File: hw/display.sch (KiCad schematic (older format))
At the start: 22 parts, among them J1 AMPSEAL_8_POS_776275-1, J4 HEADER_MOLEX_52207-0433, J5 HEADER_MOLEX_54104-4031, U1 MCP2551_SOIC8, U2 ALLIANCE_AS4C4M16SA_TSOP_II, U3 WINDBOND_W25Q32FV_SOIC8_W, U6 MOSFET-N_2N7002W, X2 XTAL_ABS25-32.768KHZ-T, X3 BUZZER_PKM13EPYH4002-B0

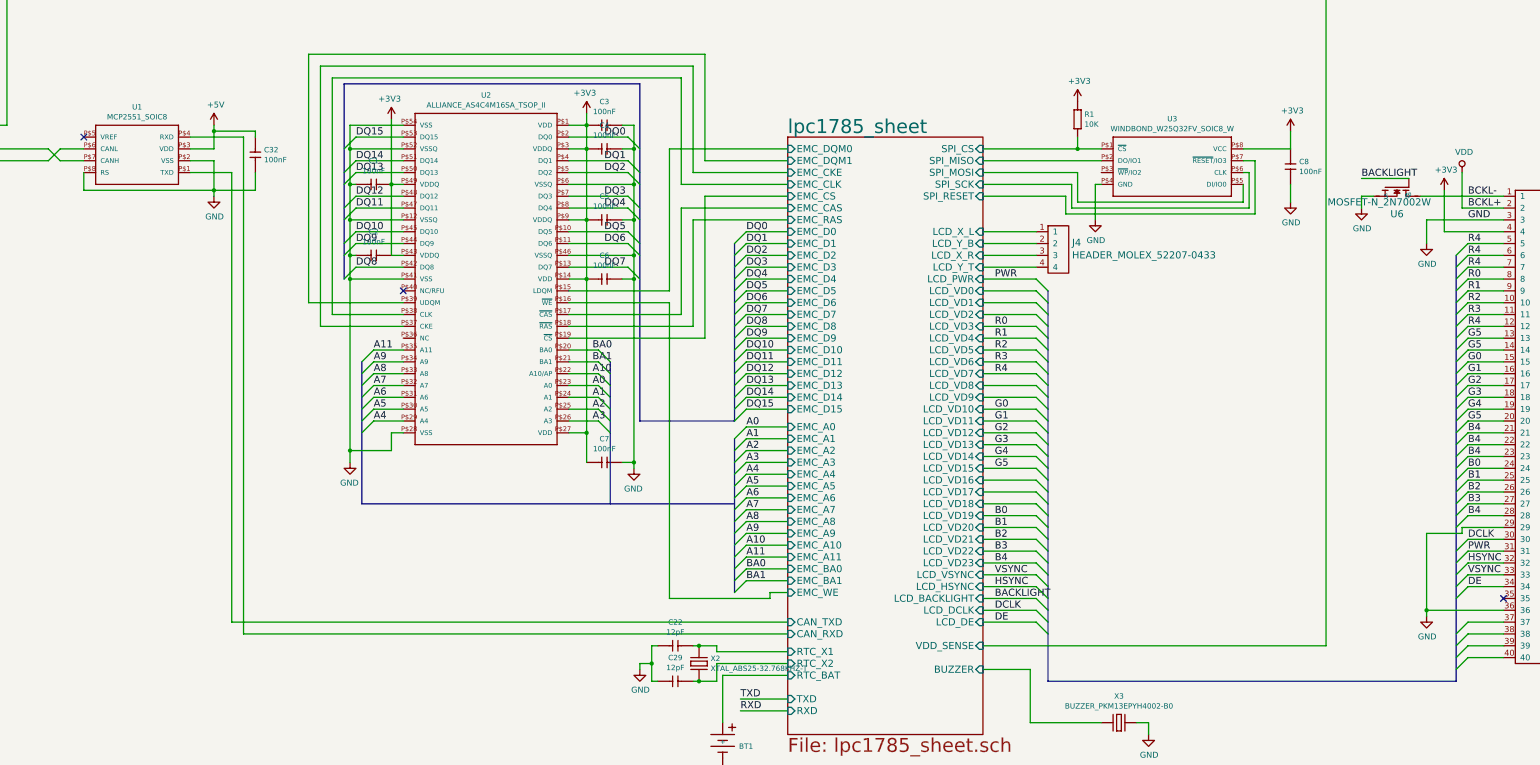
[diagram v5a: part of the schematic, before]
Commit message: Implementing notifications. not tested!
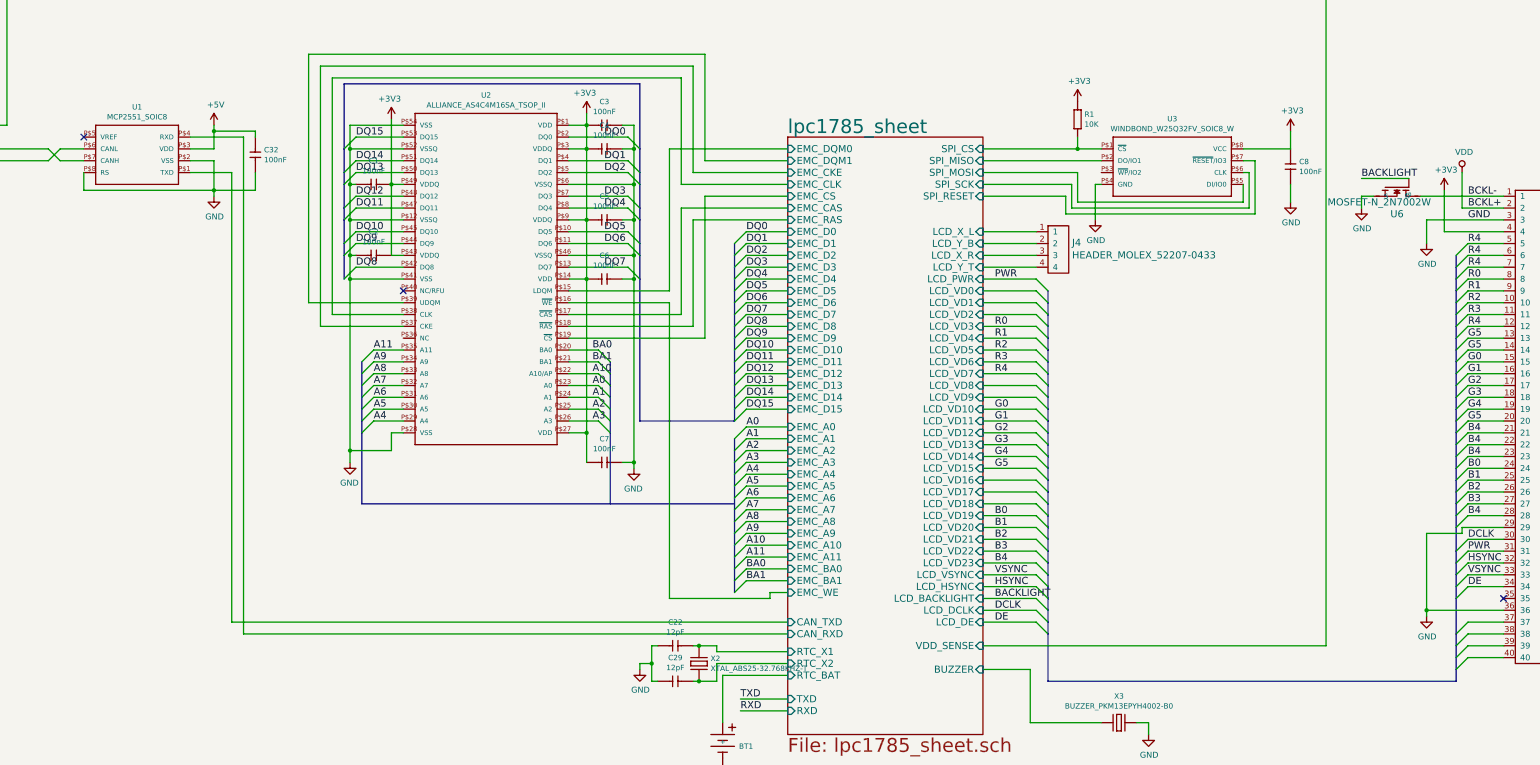
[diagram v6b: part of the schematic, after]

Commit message: multiple bug fixes, uv terminal SDO interface
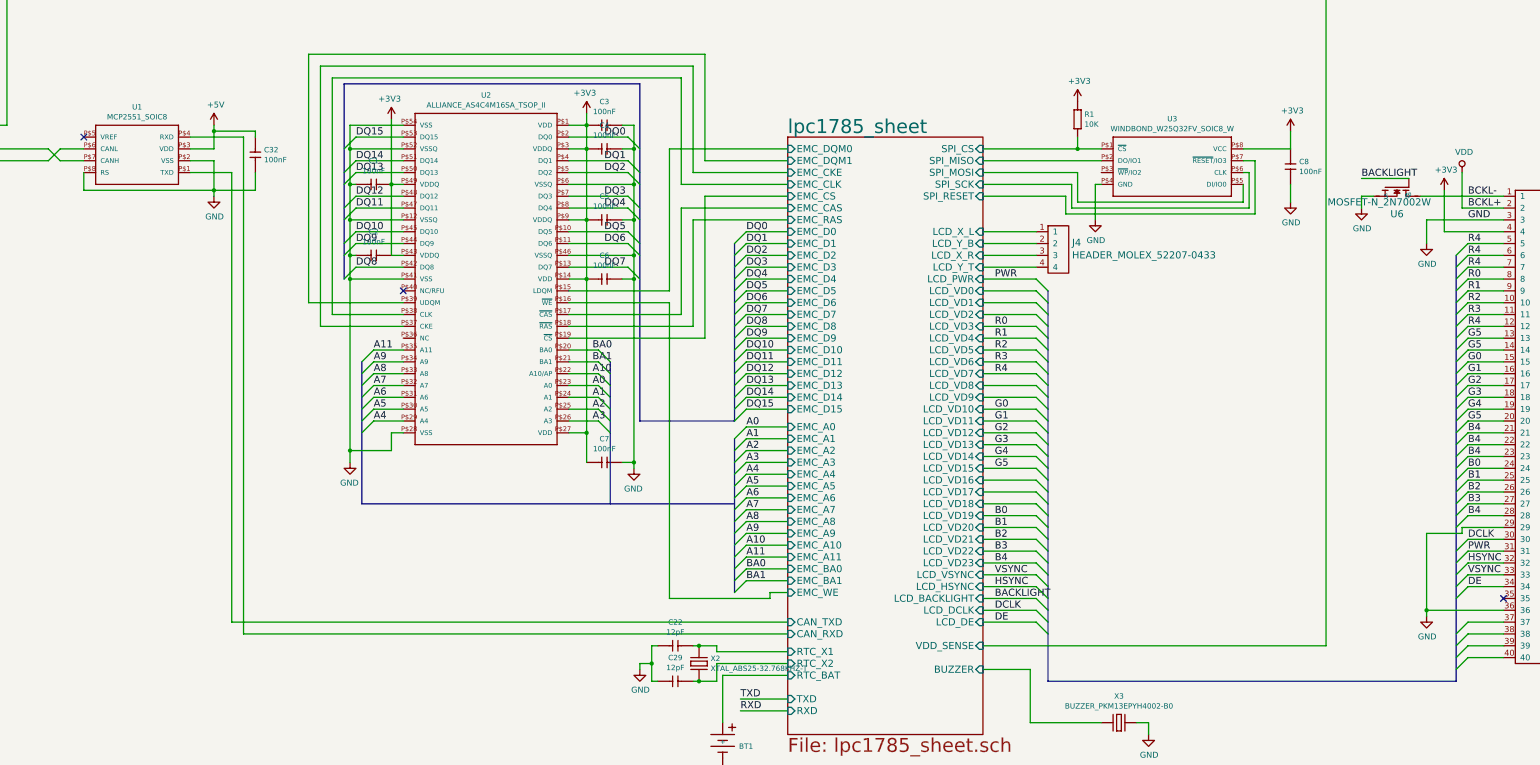
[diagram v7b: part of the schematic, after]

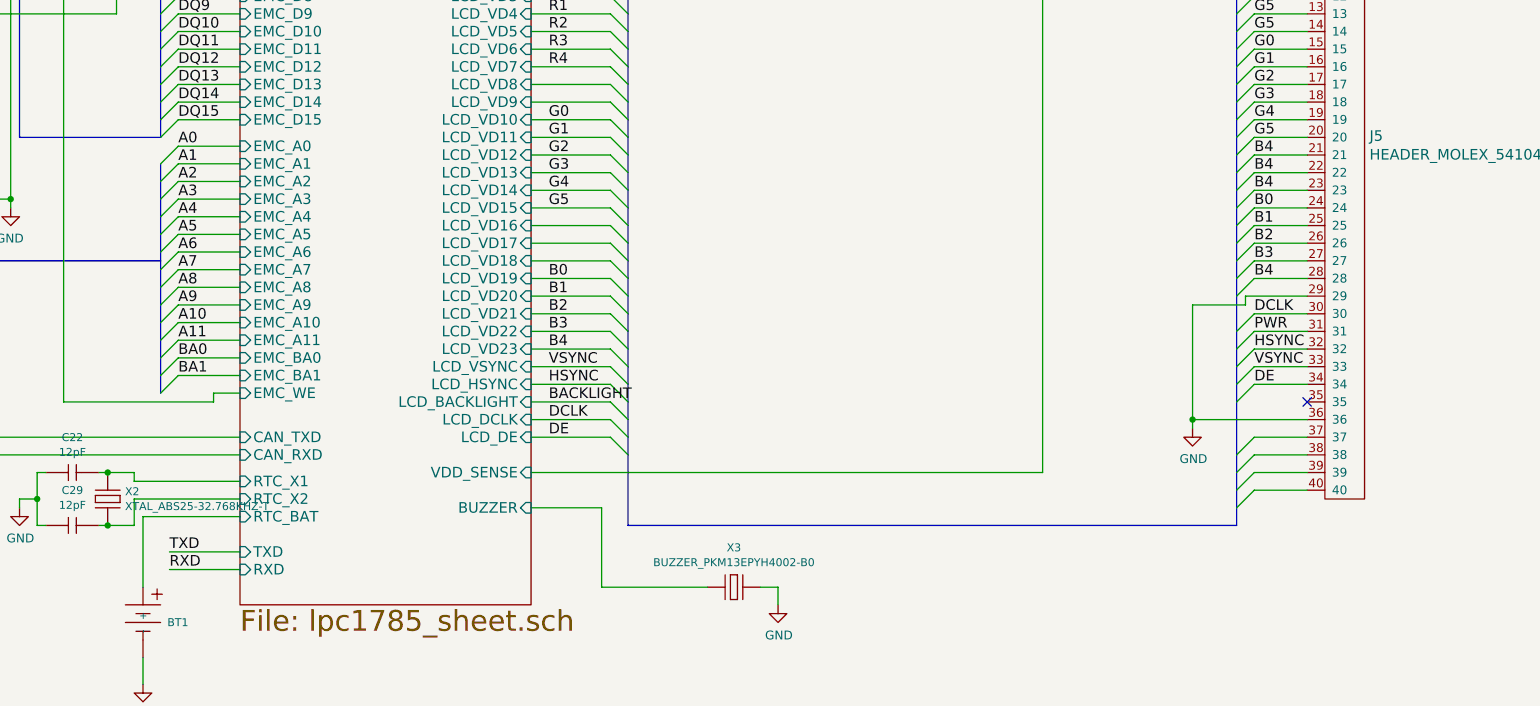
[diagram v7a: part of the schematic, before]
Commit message: starting to design hw 5.0, with variable current source for LCD backlight
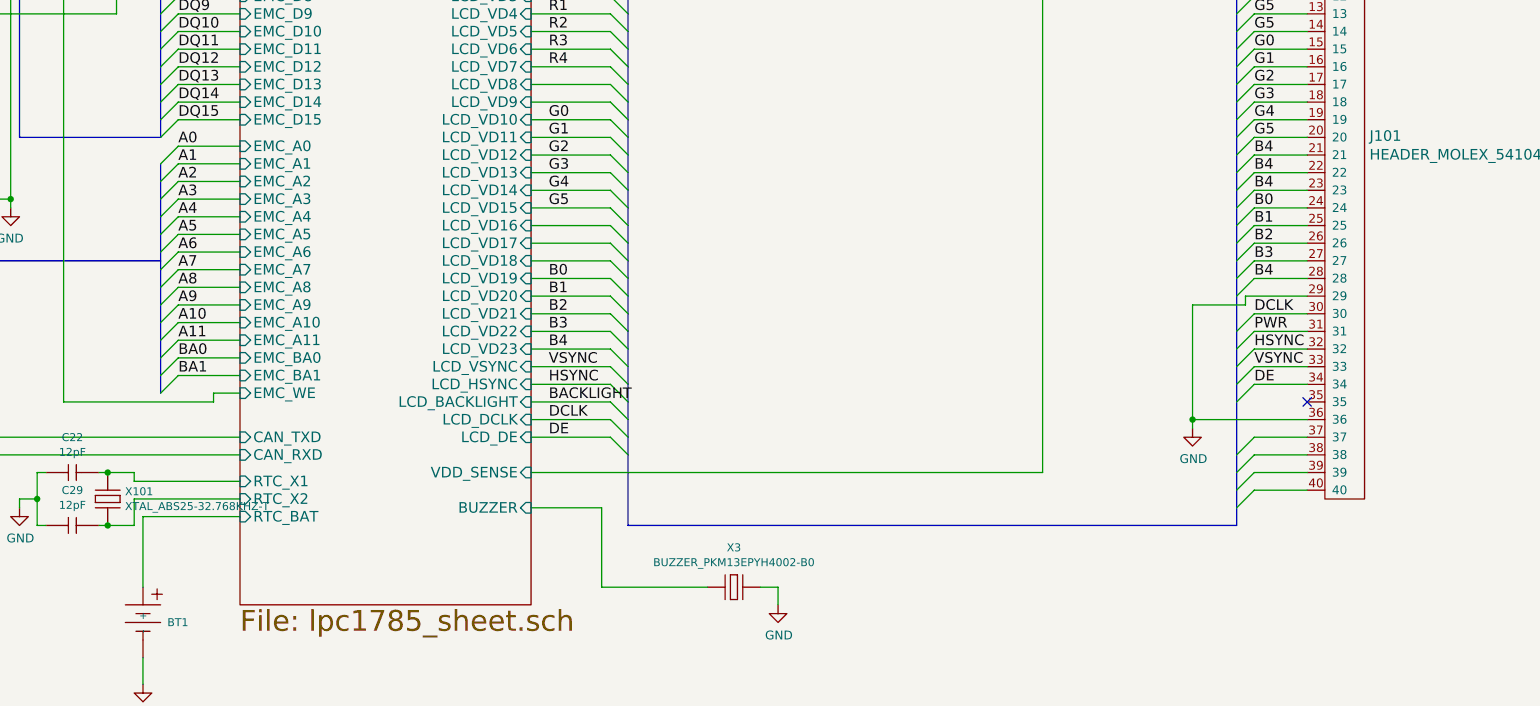
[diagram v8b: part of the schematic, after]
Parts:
- removed J5: HEADER_MOLEX_54104-4031, usevolt:HEADER_MOLEX_54104-4031, symbol HEADER_MOLEX_54104-4031
- removed X2: XTAL_ABS25-32.768KHZ-T, usevolt:XTAL_32.768KHZ-T, symbol XTAL_ABS25-32.768KHZ-T
- added J101: HEADER_MOLEX_54104-4031, usevolt:HEADER_MOLEX_54104-4031, symbol HEADER_MOLEX_54104-4031
- added X101: XTAL_ABS25-32.768KHZ-T, usevolt:XTAL_32.768KHZ-T, symbol XTAL_ABS25-32.768KHZ-T
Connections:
- net +3V3: now also J101.4
- net B0: now also J101.24
- net B1: now also J101.25
- net B2: now also J101.26
- net B3: now also J101.27
- net B4: now also J101.21, J101.22, J101.23, J101.28
- net BCKL-: now also J101.1
- net DCLK: now also J101.30
- net DE: now also J101.34
- net G0: now also J101.15
- net G1: now also J101.16
- net G2: now also J101.17
- net G3: now also J101.18
- net G4: now also J101.19
- net G5: now also J101.13, J101.14, J101.20
- net GND: now also J101.29, J101.3, J101.36
- net HSYNC: now also J101.32
- net PWR: now also J101.31
- net R0: now also J101.8
- net R1: now also J101.9
- net R2: now also J101.10
- net R3: now also J101.11
- net R4: now also J101.12, J101.5, J101.6, J101.7
- net VDD: now also J101.2
- net VSYNC: now also J101.33
- net lpc1785_sheet/RTC_X1: now also X101.1 (P$1)
- net lpc1785_sheet/RTC_X2: now also X101.4 (P$2)
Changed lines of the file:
@@
 $EndComp
 $Comp
-L +5V #PWR01
+L +5V #PWR101
 U 1 1 57BD825A
 P 3200 3000
-F 0 "#PWR01" H 3200 2850 50  0001 C CNN
+F 0 "#PWR101" H 3200 2850 50  0001 C CNN
 F 1 "+5V" H 3215 3173 50  0000 C CNN
 F 2 "" H 3200 3000 50  0000 C CNN
@@
 $EndComp
 $Comp
-L GND #PWR02
+L GND #PWR102
 U 1 1 57BD84BA
 P 3200 3600
-F 0 "#PWR02" H 3200 3350 50  0001 C CNN
+F 0 "#PWR102" H 3200 3350 50  0001 C CNN
 F 1 "GND" H 3205 3427 50  0000 C CNN
 F 2 "" H 3200 3600 50  0000 C CNN
@@
 $EndComp
 $Comp
-L +3V3 #PWR03
+L +3V3 #PWR105
 U 1 1 57C0A187
 P 6350 2900
-F 0 "#PWR03" H 6350 2750 50  0001 C CNN
+F 0 "#PWR105" H 6350 2750 50  0001 C CNN
 F 1 "+3V3" H 6365 3073 50  0000 C CNN
 F 2 "" H 6350 2900 50  0000 C CNN
@@
 $EndComp
 $Comp
-L +3V3 #PWR04
+L +3V3 #PWR104
 U 1 1 57C0A3E9
 P 4700 2950
-F 0 "#PWR04" H 4700 2800 50  0001 C CNN
+F 0 "#PWR104" H 4700 2800 50  0001 C CNN
 F 1 "+3V3" H 4715 3123 50  0000 C CNN
 F 2 "" H 4700 2950 50  0000 C CNN
@@
 $EndComp
 $Comp
-L GND #PWR05
+L GND #PWR106
 U 1 1 57C0A773
 P 6750 5900
-F 0 "#PWR05" H 6750 5650 50  0001 C CNN
+F 0 "#PWR106" H 6750 5650 50  0001 C CNN
 F 1 "GND" H 6755 5727 50  0000 C CNN
 F 2 "" H 6750 5900 50  0000 C CNN
@@
 $EndComp
 $Comp
-L GND #PWR06
+L GND #PWR103
 U 1 1 57C0BFBA
 P 4350 5850
-F 0 "#PWR06" H 4350 5600 50  0001 C CNN
+F 0 "#PWR103" H 4350 5600 50  0001 C CNN
 F 1 "GND" H 4355 5677 50  0000 C CNN
 F 2 "" H 4350 5850 50  0000 C CNN
@@
 $EndComp
 $Comp
-L GND #PWR07
+L GND #PWR110
 U 1 1 57C58382
 P 10650 3800
-F 0 "#PWR07" H 10650 3550 50  0001 C CNN
+F 0 "#PWR110" H 10650 3550 50  0001 C CNN
 F 1 "GND" H 10655 3627 50  0000 C CNN
 F 2 "" H 10650 3800 50  0000 C CNN
@@
 $EndComp
 $Comp
-L +3V3 #PWR08
+L +3V3 #PWR112
 U 1 1 57C588D1
 P 12300 3050
-F 0 "#PWR08" H 12300 2900 50  0001 C CNN
+F 0 "#PWR112" H 12300 2900 50  0001 C CNN
 F 1 "+3V3" H 12315 3223 50  0000 C CNN
 F 2 "" H 12300 3050 50  0000 C CNN
@@
 $EndComp
 $Comp
-L GND #PWR09
+L GND #PWR113
 U 1 1 57C596F8
 P 12300 3650
-F 0 "#PWR09" H 12300 3400 50  0001 C CNN
+F 0 "#PWR113" H 12300 3400 50  0001 C CNN
 F 1 "GND" H 12305 3477 50  0000 C CNN
 F 2 "" H 12300 3650 50  0000 C CNN
@@
 $EndComp
 $Comp
-L +3V3 #PWR010
+L +3V3 #PWR109
 U 1 1 57C5A7BF
 P 10500 2800
-F 0 "#PWR010" H 10500 2650 50  0001 C CNN
+F 0 "#PWR109" H 10500 2650 50  0001 C CNN
 F 1 "+3V3" H 10515 2973 50  0000 C CNN
 F 2 "" H 10500 2800 50  0000 C CNN
@@
 GND
 $Comp
-L +3V3 #PWR011
+L +3V3 #PWR117
 U 1 1 57BF31A5
 P 13600 3550
-F 0 "#PWR011" H 13600 3400 50  0001 C CNN
+F 0 "#PWR117" H 13600 3400 50  0001 C CNN
 F 1 "+3V3" H 13615 3723 50  0000 C CNN
 F 2 "" H 13600 3550 50  0000 C CNN
@@
 $EndComp
 $Comp
-L GND #PWR012
+L GND #PWR115
 U 1 1 57BF38B7
 P 13450 4000
-F 0 "#PWR012" H 13450 3750 50  0001 C CNN
+F 0 "#PWR115" H 13450 3750 50  0001 C CNN
 F 1 "GND" H 13455 3827 50  0000 C CNN
 F 2 "" H 13450 4000 50  0000 C CNN
@@
 B4
 $Comp
-L GND #PWR013
+L GND #PWR116
 U 1 1 57BFF748
 P 13450 7150
-F 0 "#PWR013" H 13450 6900 50  0001 C CNN
+F 0 "#PWR116" H 13450 6900 50  0001 C CNN
 F 1 "GND" H 13455 6977 50  0000 C CNN
 F 2 "" H 13450 7150 50  0000 C CNN
@@
 NoConn ~ 14100 7000
 $Comp
-L VDD #PWR014
+L VDD #PWR118
 U 1 1 57C283B6
 P 13750 3400
-F 0 "#PWR014" H 13750 3250 50  0001 C CNN
+F 0 "#PWR118" H 13750 3250 50  0001 C CNN
 F 1 "VDD" H 13767 3573 50  0000 C CNN
 F 2 "" H 13750 3400 50  0000 C CNN
@@
 F79 "RTC_X1" I L 8050 7450 60
 F80 "VDD_SENSE" I R 9700 7400 60
-F81 "TXD" I L 8050 7850 60
-F82 "RXD" I L 8050 7950 60
 F83 "SPI_MOSI" I R 9700 3400 60
 F84 "SPI_MISO" I R 9700 3300 60
@@
 $EndComp
 $Comp
-L HEADER_MOLEX_54104-4031 J5
-U 1 1 57C476E2
-P 14250 5050
-F 0 "J5" H 14453 4608 60  0000 L CNN
-F 1 "HEADER_MOLEX_54104-4031" H 14453 4502 60  0000 L CNN
-F 2 "usevolt:HEADER_MOLEX_54104-4031" H 14350 6700 60  0001 C CNN
-F 3 "http://www.farnell.com/datasheets/1875244.pdf?_ga=1.223199835.1948984246.1460023966" H 14225 7025 60  0001 C CNN
-F 4 "1757126" H 14125 6975 60  0001 C CNN "1st Source Part Number"
-F 5 "54104-4031" H 14100 6850 60  0001 C CNN "Manufacturer Part Number"
-F 6 "Farnell" H 14125 6925 60  0001 C CNN "1st Source"
-F 7 "MOLEX" H 14125 6775 60  0001 C CNN "Manufacturer"
-	1    14250 5050
-	1    0    0    -1
-$EndComp
-$Comp
 L BATTERY_HOLDER_CH7410-2032LFSMD BT1
 U 1 1 57C449B5
@@
 $EndComp
 $Comp
-L GND #PWR015
+L GND #PWR108
 U 1 1 57C44DCF
 P 7500 8600
-F 0 "#PWR015" H 7500 8350 50  0001 C CNN
+F 0 "#PWR108" H 7500 8350 50  0001 C CNN
 F 1 "GND" H 7505 8427 50  0000 C CNN
 F 2 "" H 7500 8600 50  0000 C CNN
@@
 $EndComp
 $Comp
-L GND #PWR016
+L GND #PWR107
 U 1 1 57C4DF04
 P 6800 7600
-F 0 "#PWR016" H 6800 7350 50  0001 C CNN
+F 0 "#PWR107" H 6800 7350 50  0001 C CNN
 F 1 "GND" H 6805 7427 50  0000 C CNN
 F 2 "" H 6800 7600 50  0000 C CNN
@@
 	1    6800 7600
 	1    0    0    -1
-$EndComp
-$Comp
-L XTAL_ABS25-32.768KHZ-T X2
-U 1 1 57C465F9
-P 7300 7600
-F 0 "X2" V 7208 7698 45  0000 L CNN
-F 1 "XTAL_ABS25-32.768KHZ-T" V 7292 7698 45  0000 L CNN
-F 2 "usevolt:XTAL_32.768KHZ-T" H 7330 7750 20  0001 C CNN
-F 3 "http://www.abracon.com/Resonators/abs25.pdf" H 7320 7620 60  0001 C CNN
-F 4 "1611824" H 7920 8220 60  0001 C CNN "2nd Source Part Number"
-F 5 "535-9166-1-ND" H 7720 8020 60  0001 C CNN "1st Source Part Number"
-F 6 "Abracon LLC" H 7420 7720 60  0001 C CNN "Manufacturer"
-F 7 "ABS25-32.768KHZ-T" H 7520 7820 60  0001 C CNN "Manufacturer Part Number"
-F 8 "Digi-Key" H 7620 7920 60  0001 C CNN "1st Source"
-F 9 "Farnell" H 7820 8120 60  0001 C CNN "2nd Source"
-	1    7300 7600
-	0    1    1    0
 $EndComp
 $Comp
@@
 $EndComp
 $Comp
-L GND #PWR018
+L GND #PWR111
 U 1 1 57C7D7AA
 P 11100 8150
-F 0 "#PWR018" H 11100 7900 50  0001 C CNN
+F 0 "#PWR111" H 11100 7900 50  0001 C CNN
 F 1 "GND" H 11105 7977 50  0000 C CNN
 F 2 "" H 11100 8150 50  0000 C CNN
@@
 BACKLIGHT
 $Comp
-L GND #PWR019
+L GND #PWR114
 U 1 1 57C8B821
 P 12900 3700
-F 0 "#PWR019" H 12900 3450 50  0001 C CNN
+F 0 "#PWR114" H 12900 3450 50  0001 C CNN
 F 1 "GND" H 12905 3527 50  0000 C CNN
 F 2 "" H 12900 3700 50  0000 C CNN
@@
 	-1   0    0    1
 $EndComp
-Text Label 7650 7950 0    60   ~ 0
-RXD
-Text Label 7650 7850 0    60   ~ 0
-TXD
 Wire Wire Line
 	12900 3600 13000 3600
@@
 Wire Wire Line
 	1450 3000 850  3000
-Wire Wire Line
-	8050 7850 7650 7850
-Wire Wire Line
-	7650 7950 8050 7950
+$Comp
+L HEADER_MOLEX_54104-4031 J101
+U 1 1 58F16957
+P 14250 5050
+F 0 "J101" H 14453 4608 60  0000 L CNN
+F 1 "HEADER_MOLEX_54104-4031" H 14453 4502 60  0000 L CNN
+F 2 "usevolt:HEADER_MOLEX_54104-4031" H 14350 6700 60  0001 C CNN
+F 3 "http://www.farnell.com/datasheets/1875244.pdf?_ga=1.223199835.1948984246.1460023966" H 14225 7025 60  0001 C CNN
+F 4 "1757126" H 14125 6975 60  0001 C CNN "1st Source Part Number"
+F 5 "54104-4031" H 14100 6850 60  0001 C CNN "Manufacturer Part Number"
+F 6 "Farnell" H 14125 6925 60  0001 C CNN "1st Source"
+F 7 "MOLEX" H 14125 6775 60  0001 C CNN "Manufacturer"
+	1    14250 5050
+	1    0    0    -1
+$EndComp
+$Comp
+L XTAL_ABS25-32.768KHZ-T X101
+U 1 1 58F353CC
+P 7300 7600
+F 0 "X101" V 7208 7698 45  0000 L CNN
+F 1 "XTAL_ABS25-32.768KHZ-T" V 7292 7698 45  0000 L CNN
+F 2 "usevolt:XTAL_32.768KHZ-T" H 7330 7750 20  0001 C CNN
+F 3 "http://www.abracon.com/Resonators/abs25.pdf" H 7320 7620 60  0001 C CNN
+F 4 "1611824" H 7920 8220 60  0001 C CNN "2nd Source Part Number"
+F 5 "535-9166-1-ND" H 7720 8020 60  0001 C CNN "1st Source Part Number"
+F 6 "Abracon LLC" H 7420 7720 60  0001 C CNN "Manufacturer"
+F 7 "ABS25-32.768KHZ-T" H 7520 7820 60  0001 C CNN "Manufacturer Part Number"
+F 8 "Digi-Key" H 7620 7920 60  0001 C CNN "1st Source"
+F 9 "Farnell" H 7820 8120 60  0001 C CNN "2nd Source"
+	1    7300 7600
+	0    1    1    0
+$EndComp
 $EndSCHEMATC
